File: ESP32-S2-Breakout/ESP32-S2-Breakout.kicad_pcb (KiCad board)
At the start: 2 copper layers, 61 x 30.5 mm, 35 parts, among them J1 USB_B_Micro, J3 Conn_01x23, SW1 Reset, SW2 Boot, U1 USBLC6-2SC6, U2 ESP32-S2-WROOM, U3 XC6220B331MR, Y1 32.768KHz

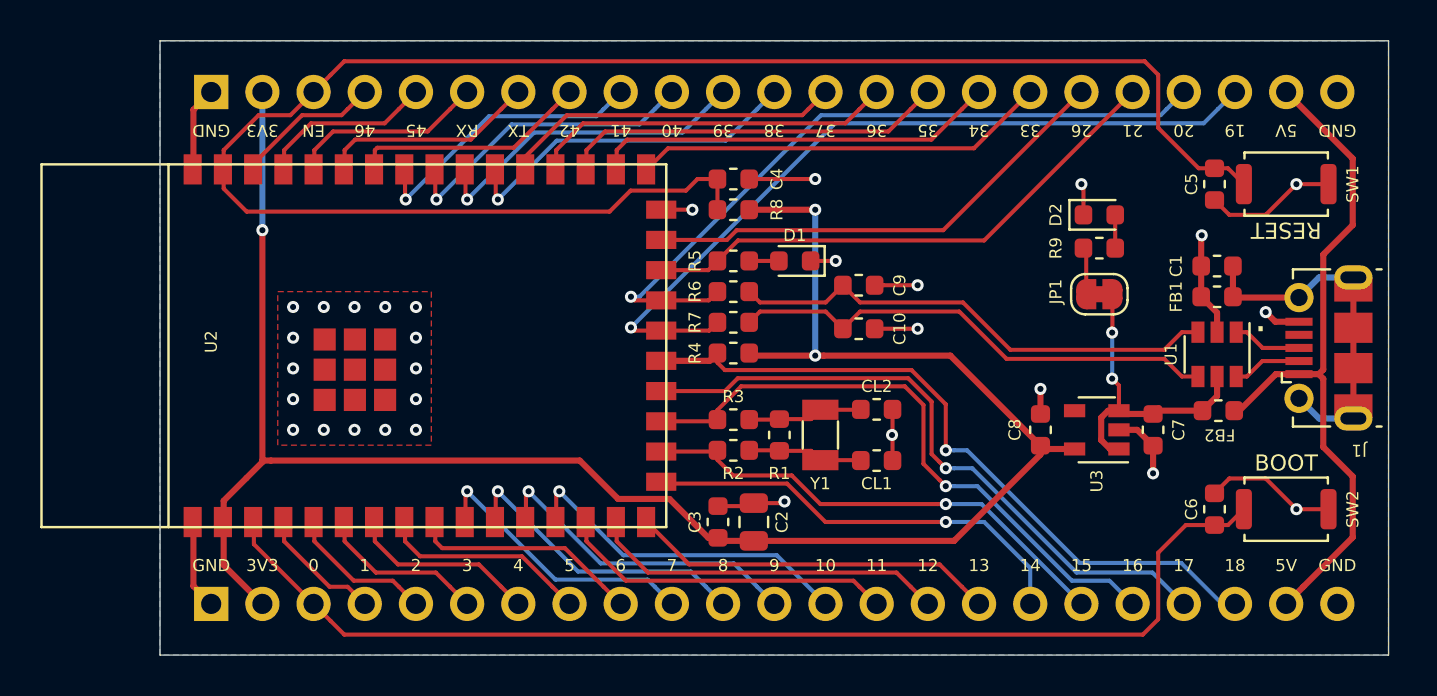
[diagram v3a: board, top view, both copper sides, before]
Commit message: Change all passives from 0603 to 0805 Add capacitor to input pin of USBLC6 Update gerbers and images
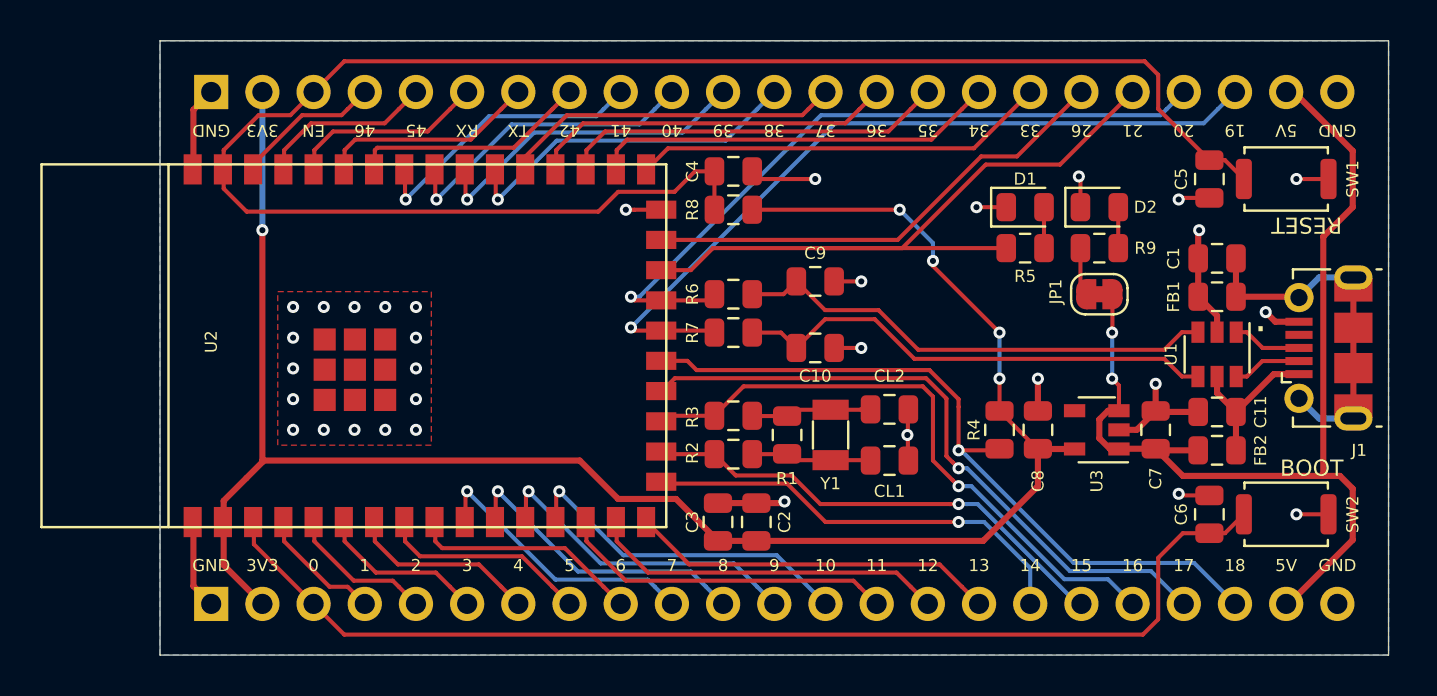
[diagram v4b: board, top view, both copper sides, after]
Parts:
- added C11: 0.1u, Capacitor_SMD:C_0805_2012Metric, F.Cu at (169.3, 102.2)
- C1, C10, C3, C4, C5, C6, C7, C8, C9, CL1, CL2: footprint Capacitor_SMD:C_0603_1608Metric -> Capacitor_SMD:C_0805_2012Metric
- D1, D2: footprint LED_SMD:LED_0603_1608Metric -> LED_SMD:LED_0805_2012Metric
- FB1, FB2: footprint Inductor_SMD:L_0603_1608Metric -> Inductor_SMD:L_0805_2012Metric
- R1, R2, R3, R4, R5, R6, R7, R8, R9: footprint Resistor_SMD:R_0603_1608Metric -> Resistor_SMD:R_0805_2012Metric
- moved R5 14.5 mm to (159.8, 94.1)
- moved R4 13.7 mm to (158.5, 103.1), turned to 270 degrees
- moved D1 11.7 mm to (159.8, 92.1), turned to 0 degrees
- moved C10 2.36 mm to (149.4, 99.1)
- moved C9 2.17 mm to (149.4, 95.8)
- moved FB2 1.97 mm to (169.3, 104.1)
- moved CL1 0.63 mm to (153.0, 104.6)
- moved CL2 0.63 mm to (153.0, 102.1)
- moved Y1 0.51 mm to (150.1, 103.4)
- moved R7 0.51 mm to (145.3, 98.3)
- moved C1 0.38 mm to (169.3, 94.6)
- moved C4 0.38 mm to (145.3, 90.3)
- moved D2 0.38 mm to (163.4, 92.1)
- moved R1 0.38 mm to (148.0, 103.4)
- moved C5 0.36 mm to (168.9, 90.7)
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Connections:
- C7 pad 1: VBUS -> +5V
- FB2 pad 1: VBUS -> +5V
- FB2 pad 2: +5V -> VBUS
- J1 pad 1: +5V -> VBUS
- JP1 pad 1: VBUS -> +5V
- U3 pad 1: VBUS -> +5V
- U3 pad 3: VBUS -> +5V
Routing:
- net +5V: track 34.2 -> 52.2 mm, vias 0 -> 2
- net /IO21: track 27.3 -> 36.5 mm
- net VBUS: track 15.8 -> 7.95 mm, vias 2 -> 0
- net GND: track 51.3 -> 46.4 mm, vias 30 -> 32
- net +3V3: track 97.9 -> 94.0 mm, vias 3 -> 5
- net /IO18: track 35.4 -> 37.0 mm
- net Net-(CL2-Pad1): track 5.75 -> 6.63 mm
- net Net-(D1-Pad2): track 1.47 -> 2.03 mm

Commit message: Update crystal passive values and readme
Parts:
- CL1, CL2: value 11p C0G -> 12p C0G
- R1: value N/C -> TBD
- R2, R3: value 220r 1% -> TBD
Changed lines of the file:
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@@
       (effects (font (size 0.6 0.6) (thickness 0.15)))
     )
-    (fp_text value "220r 1%" (at 0 1.65) (layer F.Fab)
+    (fp_text value TBD (at 0 1.65) (layer F.Fab)
       (effects (font (size 1 1) (thickness 0.15)))
     )
@@
       (effects (font (size 0.6 0.6) (thickness 0.15)))
     )
-    (fp_text value "220r 1%" (at 0 1.65) (layer F.Fab)
+    (fp_text value TBD (at 0 1.65) (layer F.Fab)
       (effects (font (size 1 1) (thickness 0.15)))
     )
@@
       (effects (font (size 0.6 0.6) (thickness 0.15)))
     )
-    (fp_text value N/C (at 0 1.65 90) (layer F.Fab)
+    (fp_text value TBD (at 0 1.65 90) (layer F.Fab)
       (effects (font (size 1 1) (thickness 0.15)))
     )
@@
       (effects (font (size 0.6 0.6) (thickness 0.15)))
     )
-    (fp_text value "11p C0G" (at 0 1.65) (layer F.Fab)
+    (fp_text value "12p C0G" (at 0 1.65) (layer F.Fab)
       (effects (font (size 1 1) (thickness 0.15)))
     )
@@
       (effects (font (size 0.6 0.6) (thickness 0.15)))
     )
-    (fp_text value "11p C0G" (at 0 1.65) (layer F.Fab)
-      (effects (font (size 1 1) (thickness 0.15)))
-    )
+    (fp_text value "12p C0G" (at 0 1.65) (layer F.Fab)
+      (effects (font (size 1 1) (thickness 0.15)))
+    )

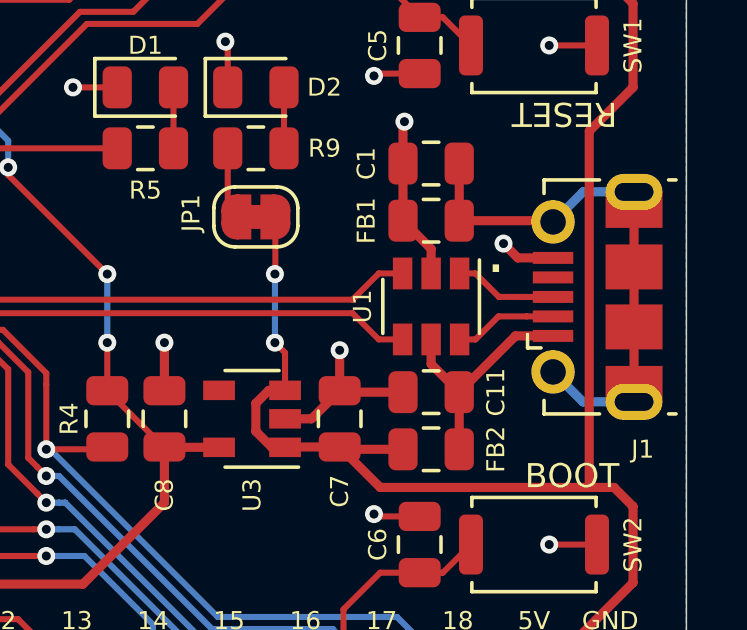
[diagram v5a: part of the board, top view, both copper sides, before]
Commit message: Update USB TVS
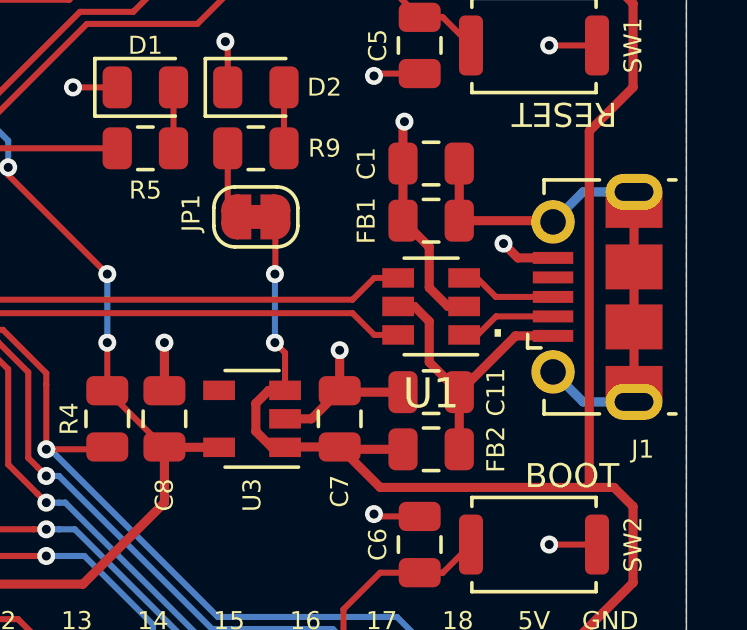
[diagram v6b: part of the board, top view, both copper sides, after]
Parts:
- CL1, CL2: value 12p C0G -> TBD
- turned U1 to 180 degrees
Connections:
- J1 pad 2: Net-(J1-Pad2) -> /D-
- J1 pad 3: Net-(J1-Pad3) -> /D+
- U1 pad 1: Net-(J1-Pad3) -> /D-
- U1 pad 3: /USB_D+ -> /D+
- U1 pad 4: /USB_D- -> /USB_D+
- U1 pad 6: Net-(J1-Pad2) -> /USB_D-
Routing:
- net Net-(J1-Pad3): track 3.44 -> 0.00 mm
- net Net-(J1-Pad2): track 3.43 -> 0.00 mm
- net /D+: track 0.00 -> 3.23 mm
- net /D-: track 0.00 -> 3.22 mm
- net VBUS: track 7.95 -> 9.83 mm
- net GND: track 46.4 -> 48.3 mm

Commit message: Rev 2/v2 update
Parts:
- added R10: 5.1k, Resistor_SMD:R_0603_1608Metric, F.Cu at (166.5, 96.5)
- added R11: 5.1k, Resistor_SMD:R_0603_1608Metric, F.Cu at (166.5, 101.6)
- C1, C10, C11, C2, C3, C4, C5, C6, C7, C8, C9: footprint Capacitor_SMD:C_0805_2012Metric -> Capacitor_SMD:C_0603_1608Metric
- CL1, CL2: value TBD -> 20p; footprint Capacitor_SMD:C_0805_2012Metric -> Capacitor_SMD:C_0603_1608Metric
- D1, D2: footprint LED_SMD:LED_0805_2012Metric -> LED_SMD:LED_0603_1608Metric
- FB1, FB2: footprint Inductor_SMD:L_0805_2012Metric -> Inductor_SMD:L_0603_1608Metric
- J1: value USB_B_Micro -> USB_C_Receptacle_USB2.0; footprint Connector_USB:USB_Micro-B_Molex-105017-0001 -> ESP32-S2-Breakout:USB_C_Receptacle_HRO_TYPE-C-31-M-12
- R1: value TBD -> N/C; footprint Resistor_SMD:R_0805_2012Metric -> Resistor_SMD:R_0603_1608Metric
- R2, R3: value TBD -> 0r; footprint Resistor_SMD:R_0805_2012Metric -> Resistor_SMD:R_0603_1608Metric
- R4, R6, R7, R8: footprint Resistor_SMD:R_0805_2012Metric -> Resistor_SMD:R_0603_1608Metric
- R5: value 750r -> 100r; footprint Resistor_SMD:R_0805_2012Metric -> Resistor_SMD:R_0603_1608Metric
- R9: value 1.6k -> 750r; footprint Resistor_SMD:R_0805_2012Metric -> Resistor_SMD:R_0603_1608Metric
- SW1, SW2: footprint Button_Switch_SMD:SW_Push_SPST_NO_Alps_SKRK -> ESP32-S2-Breakout:Alps_SKRK
- U2: footprint ESP32-S2-WROOM:ESP32-S2-WROOM -> ESP32-S2-Breakout:ESP32-S2-WROOM
- Y1: value 32.768KHz -> 32.768KHz 12.5p; footprint Crystal:Crystal_SMD_3215-2Pin_3.2x1.5mm -> ESP32-S2-Breakout:Crystal_SMD_3215-2Pin_3.2x1.5mm
- moved C7 4.04 mm to (162.2, 103.0)
- moved R5 3.90 mm to (155.9, 93.6)
- moved D1 3.87 mm to (155.9, 92.0)
- moved U3 3.82 mm to (159.5, 103.0)
- moved R9 3.68 mm to (159.8, 93.6)
- moved JP1 3.65 mm to (159.8, 96.5)
- moved D2 3.65 mm to (159.8, 92.0)
- moved C8 3.60 mm to (156.8, 103.0)
- moved U1 3.21 mm to (166.1, 99.1)
- moved R4 3.20 mm to (155.3, 103.0)
- moved FB1 3.18 mm to (166.5, 95.0), turned to 180 degrees
- moved C1 3.01 mm to (166.5, 93.5), turned to 0 degrees
- moved C11 2.92 mm to (166.5, 103.1)
- moved FB2 2.83 mm to (166.5, 104.6)
- moved C9 1.96 mm to (147.4, 95.9), turned to 270 degrees
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- renumbered e1 to J2
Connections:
- C1 pad 1: Net-(C1-Pad1) -> GND
- C1 pad 2: GND -> Net-(C1-Pad2)
- FB1 pad 1: GND -> Net-(C1-Pad2)
- FB1 pad 2: Net-(C1-Pad1) -> GND
- JP1 pad 1: +5V -> +3V3
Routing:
- net +3V3: track 94.0 -> 3.91 mm, vias 5 -> 0
- net /EN: track 85.3 -> 59.2 mm, vias 0 -> 3
- net Net-(C1-Pad2): track 0.00 -> 22.4 mm
- net Net-(C1-Pad1): track 17.7 -> 0.00 mm
- net GND: track 48.3 -> 63.4 mm, vias 32 -> 31
- net VBUS: track 9.83 -> 19.8 mm, vias 0 -> 2
- net /IO15: track 23.9 -> 29.9 mm
- net +5V: track 52.2 -> 57.9 mm, vias 2 -> 0
- net /IO0: track 56.3 -> 60.1 mm, vias 0 -> 2
- net /USB_D-: track 24.0 -> 20.3 mm
- net /USB_D+: track 23.9 -> 20.3 mm
- net Net-(J1-PadA5): track 0.00 -> 3.41 mm
- net Net-(J1-PadB5): track 0.00 -> 3.21 mm
- net /IO12: track 17.7 -> 20.6 mm, vias 0 -> 1
- net /IO16: track 30.4 -> 33.3 mm
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- added copper zone on F.Cu, net +3V3
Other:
- net class Default: trace_width 0.25 -> 0.2032; via_dia 0.8 -> 0.6; via_drill 0.4 -> 0.3
- rule pad_to_mask_clearance: 0.051 -> 0
- board text added: "ESP32-S2 Breakout github/eggsampler v2 Feb 2021"
- board text removed: "ESP32-S2 Breakout github/eggsampler v1 03-20"
